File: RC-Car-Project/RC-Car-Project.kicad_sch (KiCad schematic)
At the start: 4 parts

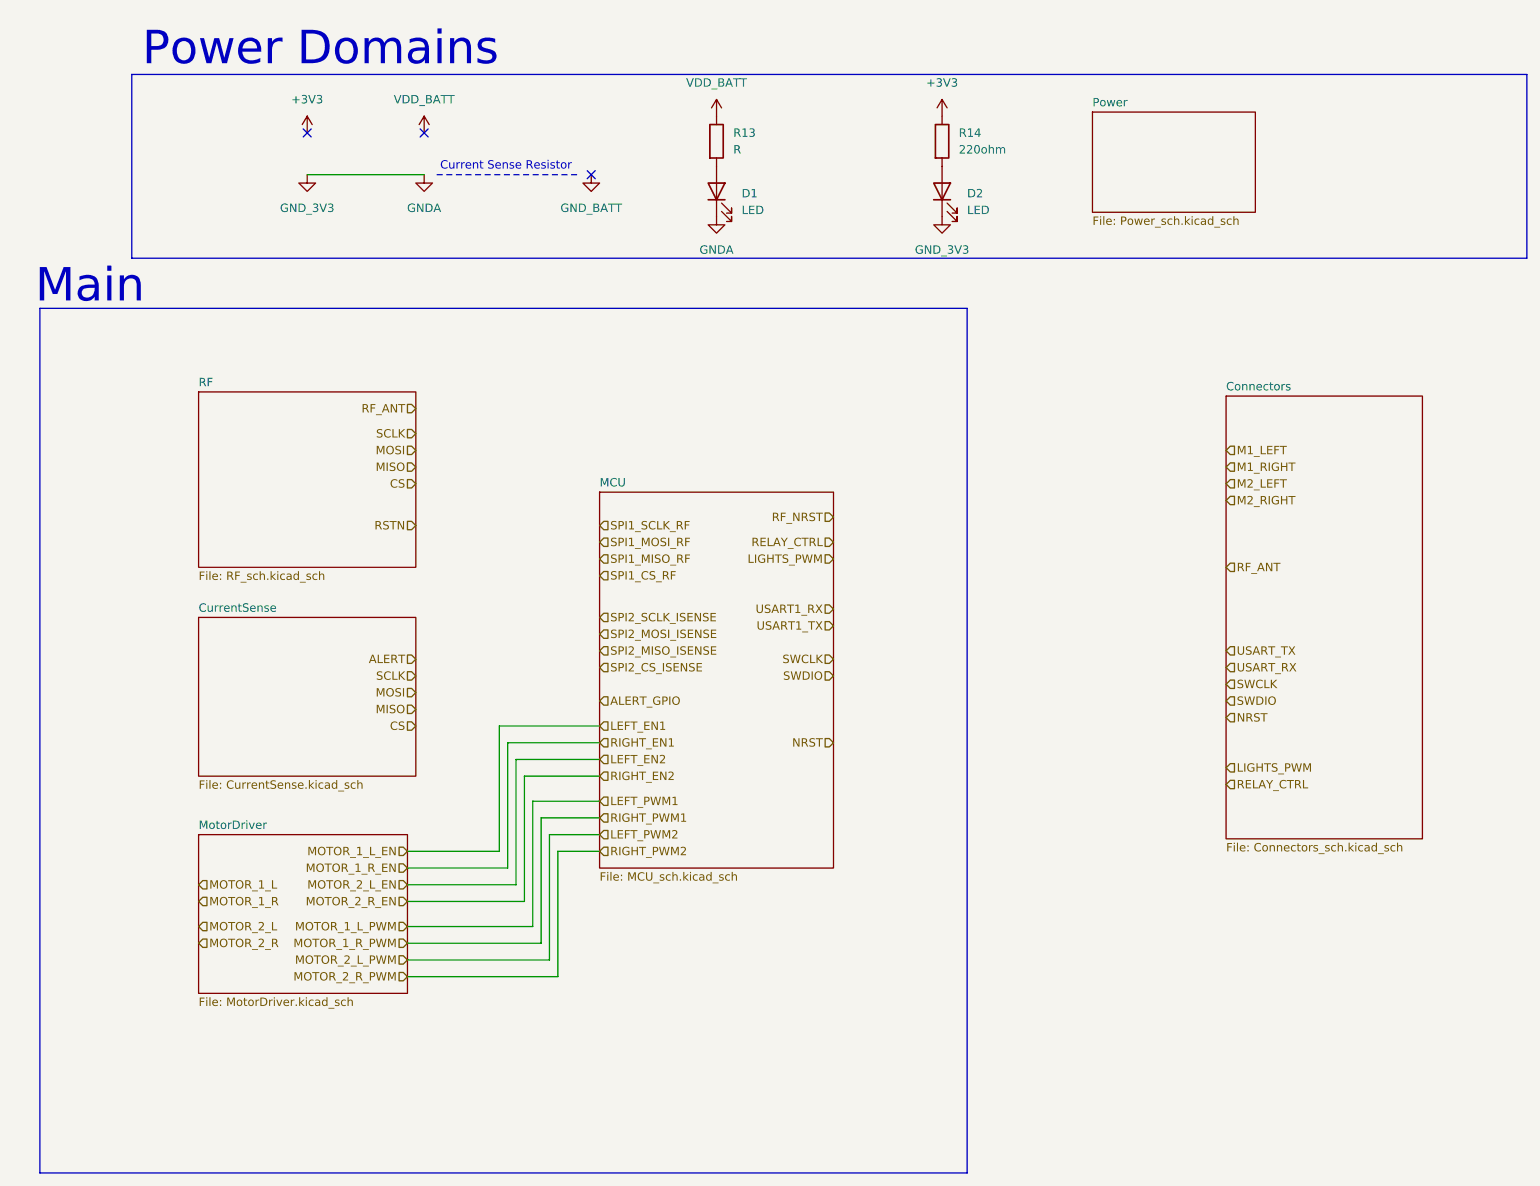
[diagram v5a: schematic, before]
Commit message: Added footprints + final parts. (Need to finish buck converter next)
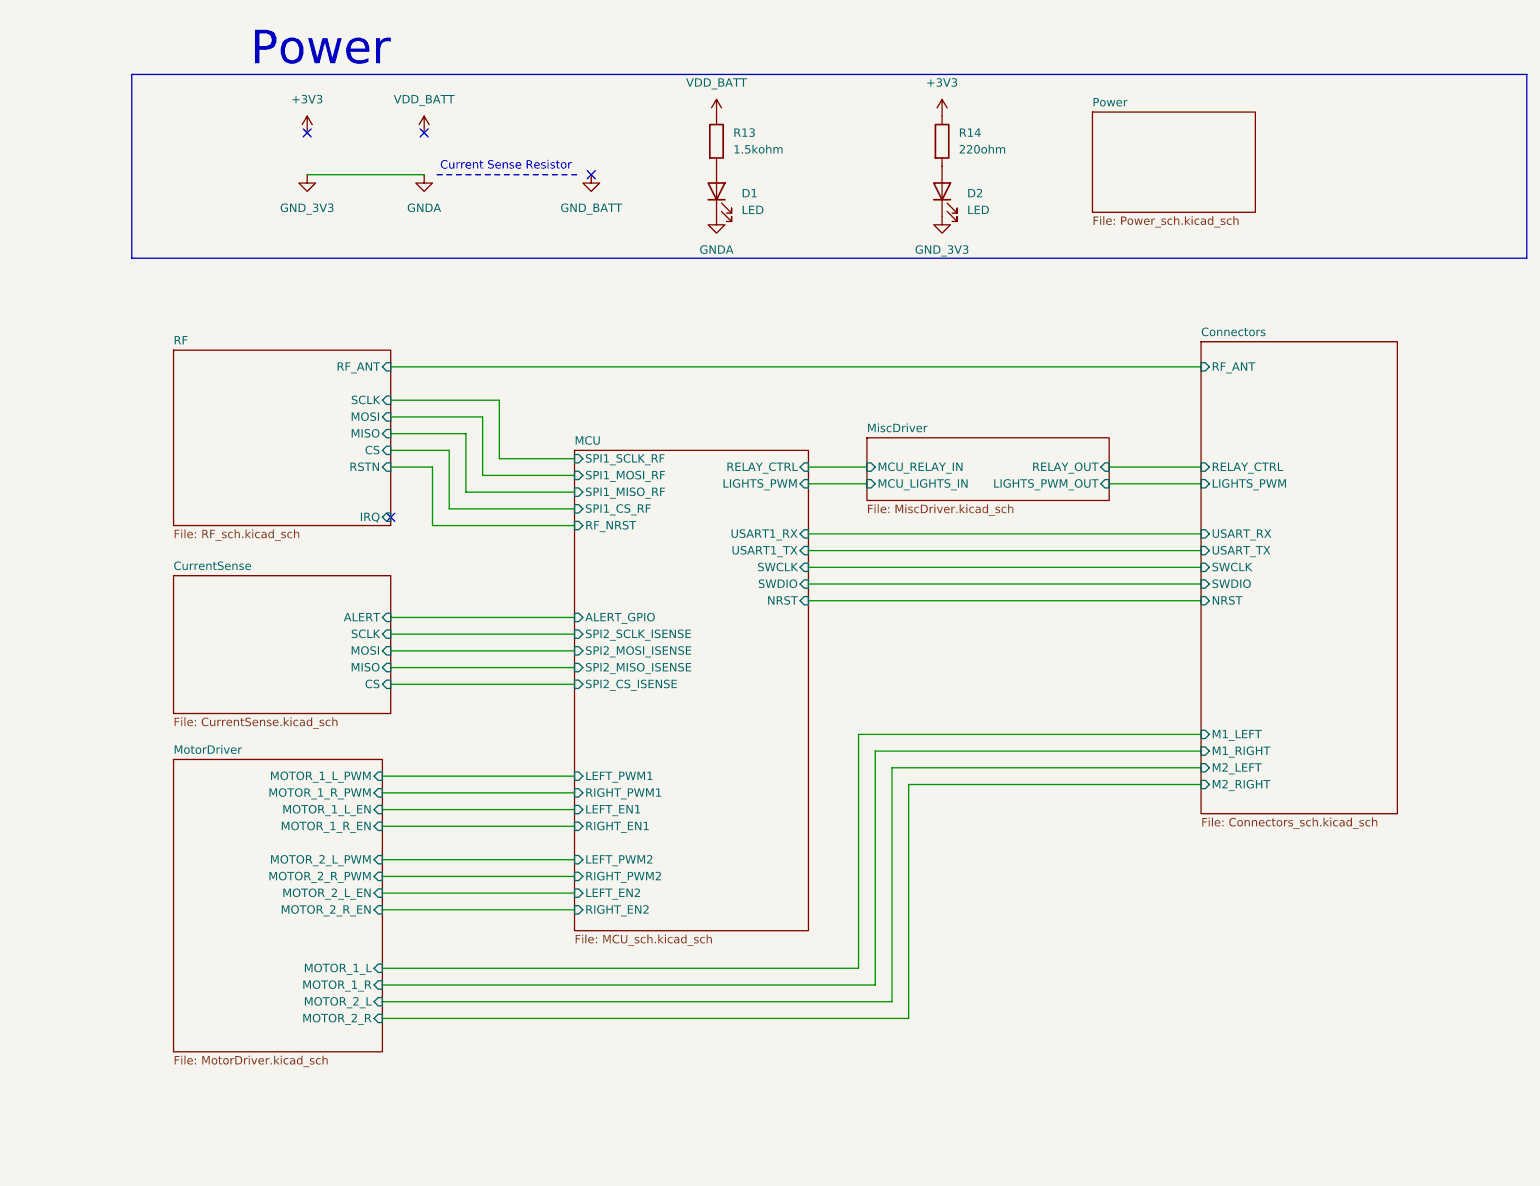
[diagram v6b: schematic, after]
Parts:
- D1, D2: footprint (none) -> LED_SMD:LED_0201_0603Metric
- R13: value R -> 1.5kohm; footprint (none) -> Resistor_SMD:R_0201_0603Metric
- R14: footprint (none) -> Resistor_SMD:R_0201_0603Metric
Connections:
- no-connect marks 3 -> 4
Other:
- added sheet MiscDriver (MiscDriver.kicad_sch)
- sheet Connectors ports: added LIGHTS_PWM, M1_LEFT, M1_RIGHT, M2_LEFT, M2_RIGHT, NRST, RELAY_CTRL, RF_ANT, SWCLK, SWDIO, USART_RX, USART_TX; removed none
- sheet CurrentSense ports: added ALERT, CS, MISO, MOSI, SCLK; removed none
- sheet MCU ports: added ALERT_GPIO, LEFT_EN1, LEFT_EN2, LEFT_PWM1, LEFT_PWM2, LIGHTS_PWM, NRST, RELAY_CTRL, RF_NRST, RIGHT_EN1, RIGHT_EN2, RIGHT_PWM1, RIGHT_PWM2, SPI1_CS_RF, SPI1_MISO_RF, SPI1_MOSI_RF, SPI1_SCLK_RF, SPI2_CS_ISENSE, SPI2_MISO_ISENSE, SPI2_MOSI_ISENSE, SPI2_SCLK_ISENSE, SWCLK, SWDIO, USART1_RX, USART1_TX; removed none
- sheet MotorDriver ports: added MOTOR_1_L, MOTOR_1_L_EN, MOTOR_1_L_PWM, MOTOR_1_R, MOTOR_1_R_EN, MOTOR_1_R_PWM, MOTOR_2_L, MOTOR_2_L_EN, MOTOR_2_L_PWM, MOTOR_2_R, MOTOR_2_R_EN, MOTOR_2_R_PWM; removed none
- sheet RF ports: added CS, IRQ, MISO, MOSI, RF_ANT, RSTN, SCLK; removed none
- note added: "Power"
- note removed: "Main"
- note removed: "Power Domains"

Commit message: Add thermo adc and camera
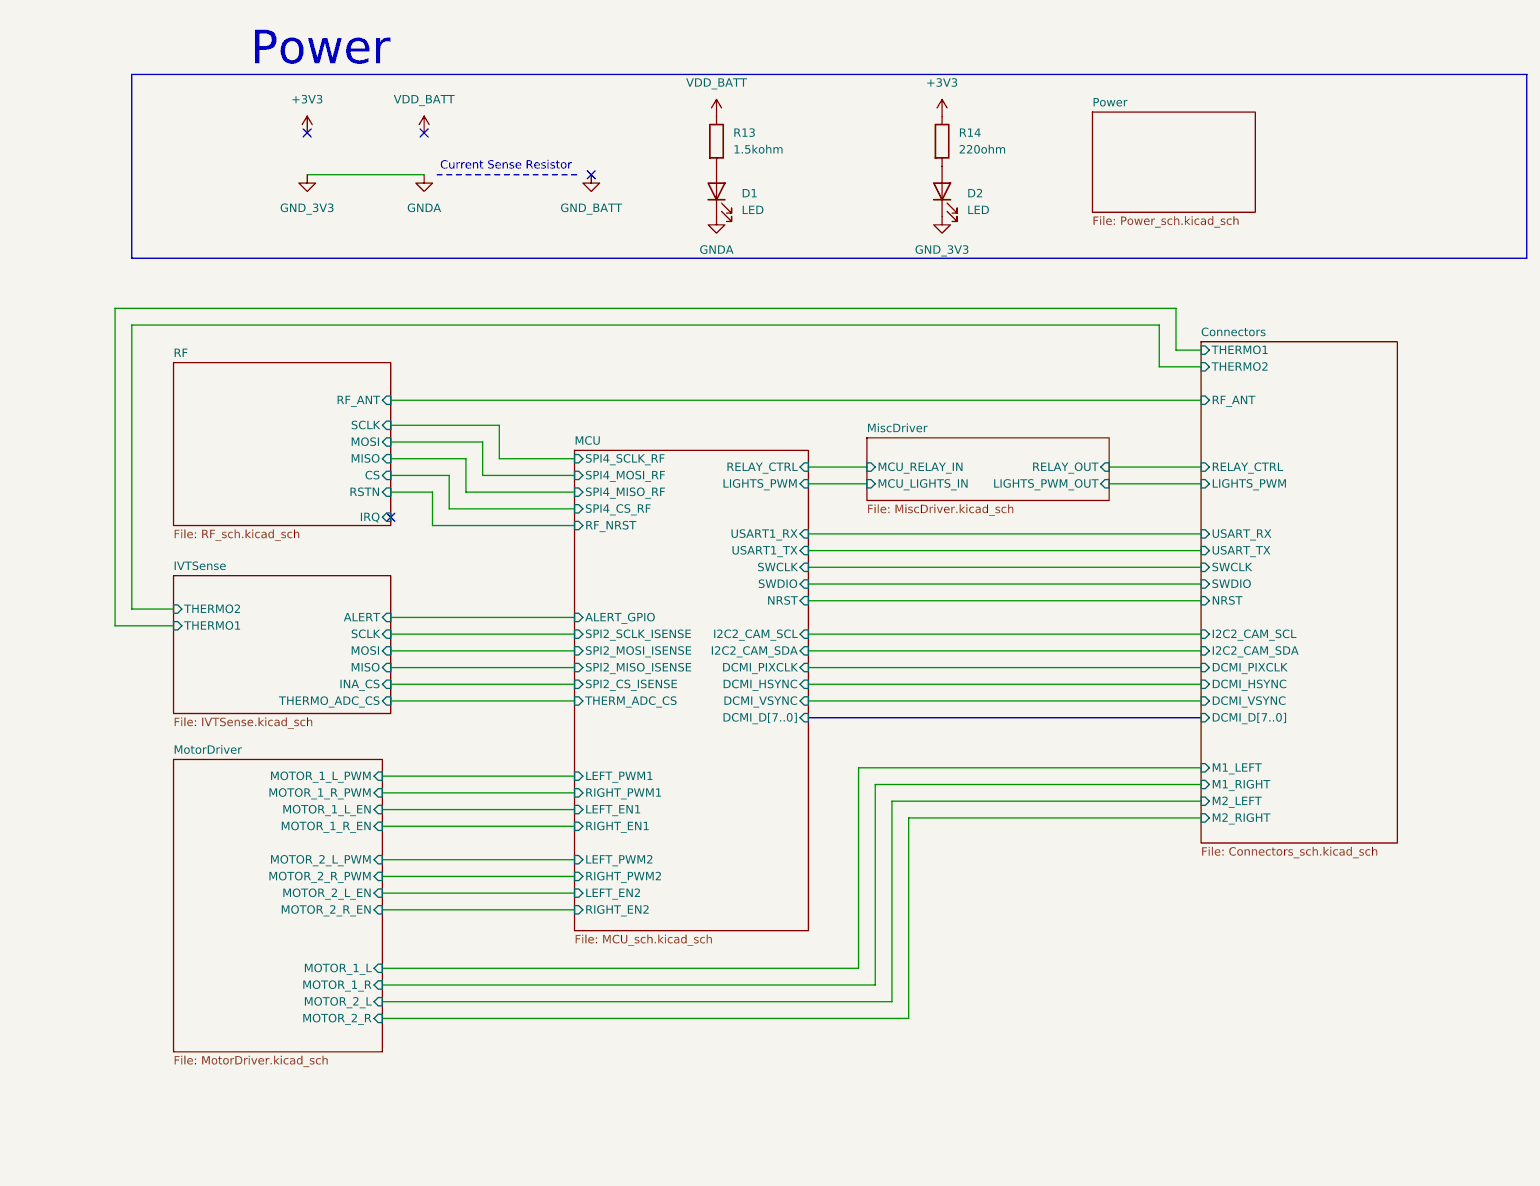
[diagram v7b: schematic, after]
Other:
- sheet CurrentSense renamed IVTSense
- sheet Connectors ports: added DCMI_D[7..0], DCMI_HSYNC, DCMI_PIXCLK, DCMI_VSYNC, I2C2_CAM_SCL, I2C2_CAM_SDA, THERMO1, THERMO2; removed none
- sheet IVTSense: file CurrentSense.kicad_sch -> IVTSense.kicad_sch
- sheet IVTSense ports: added INA_CS, THERMO1, THERMO2, THERMO_ADC_CS; removed CS
- sheet MCU ports: added DCMI_D[7..0], DCMI_HSYNC, DCMI_PIXCLK, DCMI_VSYNC, I2C2_CAM_SCL, I2C2_CAM_SDA, SPI4_CS_RF, SPI4_MISO_RF, SPI4_MOSI_RF, SPI4_SCLK_RF, THERM_ADC_CS; removed SPI1_CS_RF, SPI1_MISO_RF, SPI1_MOSI_RF, SPI1_SCLK_RF

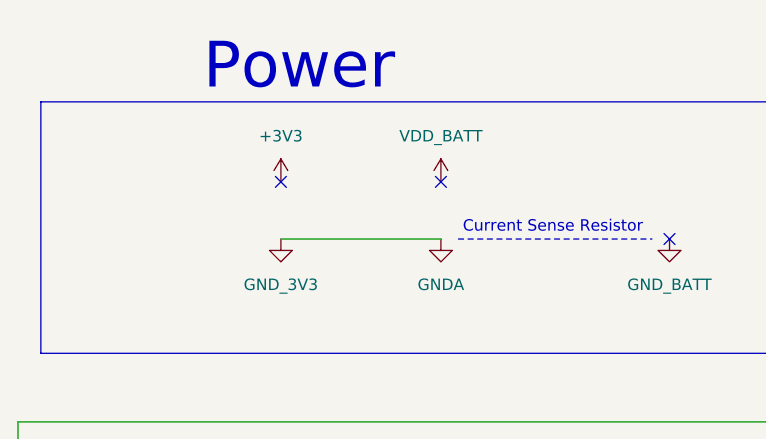
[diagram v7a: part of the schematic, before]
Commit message: Add 12V buck
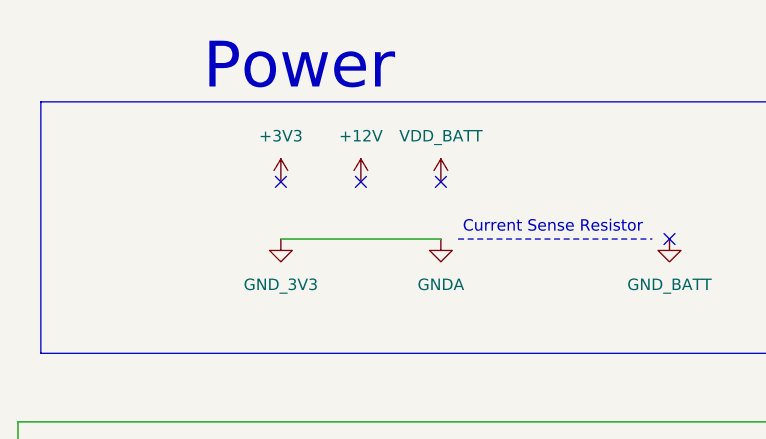
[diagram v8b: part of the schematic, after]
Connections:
- no-connect marks 4 -> 5
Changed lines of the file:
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@@
+	)
+	(no_connect
+		(at 81.28 34.29)
 	)
 	(no_connect
@@
 					(unit 1)
 				)
+			)
+		)
+	)
+	(symbol
+		(lib_id "power:+3V3")
+		(at 81.28 34.29 0)
+		(unit 1)
+		(exclude_from_sim no)
+		(in_bom yes)
+		(on_board yes)
+		(dnp no)
+		(fields_autoplaced yes)
+		(property "Reference" "#PWR012"
+			(at 81.28 38.1 0)
+			(effects
+				(font
+					(size 1.27 1.27)
+				)
+				(hide yes)
+			)
+		)
+		(property "Value" "+12V"
+			(at 81.28 29.21 0)
+			(effects
+				(font
+					(size 1.27 1.27)
+				)
+			)
+		)
+		(property "Footprint" ""
+			(at 81.28 34.29 0)
+			(effects
+				(font
+					(size 1.27 1.27)
+				)
+				(hide yes)
+			)
+		)
+		(property "Datasheet" ""
+			(at 81.28 34.29 0)
+			(effects
+				(font
+					(size 1.27 1.27)
+				)
+				(hide yes)
+			)
+		)
+		(property "Description" "Power symbol creates a global label with name \"+3V3\""
+			(at 81.28 34.29 0)
+			(effects
+				(font
+					(size 1.27 1.27)
+				)
+				(hide yes)
+			)
+		)
+		(pin "1"
+		)
+		(instances
+			(project "RC-Car-Project"
+				(path "/ba870fd1-751d-4755-8e1a-1ea86ca9e2f6"
+					(reference "#PWR012")
+					(unit 1)
+				)
